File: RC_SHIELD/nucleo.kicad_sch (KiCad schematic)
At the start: 1 part

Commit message: footprints assigned
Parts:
- A1: footprint NUCLEO-F746ZG:MODULE_NUCLEO-F746ZG -> NUCLEO-F746ZG:MODULE_NUCLEO-F746ZG_no_arduino
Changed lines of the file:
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@@
       (effects (font (size 1.27 1.27)))
     )
-    (property "Footprint" "NUCLEO-F746ZG:MODULE_NUCLEO-F746ZG" (at 69.215 -38.1 0)
+    (property "Footprint" "NUCLEO-F746ZG:MODULE_NUCLEO-F746ZG_no_arduino" (at 69.215 -38.1 0)
       (effects (font (size 1.27 1.27)) (justify bottom) hide)
     )
@@
       (effects (font (size 1.27 1.27)))
     )
-    (property "Footprint" "NUCLEO-F746ZG:MODULE_NUCLEO-F746ZG" (at 259.715 -60.96 0)
+    (property "Footprint" "NUCLEO-F746ZG:MODULE_NUCLEO-F746ZG_no_arduino" (at 259.715 -60.96 0)
       (effects (font (size 1.27 1.27)) (justify bottom) hide)
     )
@@
       (effects (font (size 1.27 1.27)))
     )
-    (property "Footprint" "NUCLEO-F746ZG:MODULE_NUCLEO-F746ZG" (at 158.115 -37.465 0)
+    (property "Footprint" "NUCLEO-F746ZG:MODULE_NUCLEO-F746ZG_no_arduino" (at 158.115 -37.465 0)
       (effects (font (size 1.27 1.27)) (justify bottom) hide)
     )
@@
       (effects (font (size 1.27 1.27)))
     )
-    (property "Footprint" "NUCLEO-F746ZG:MODULE_NUCLEO-F746ZG" (at 70.485 55.245 0)
+    (property "Footprint" "NUCLEO-F746ZG:MODULE_NUCLEO-F746ZG_no_arduino" (at 70.485 55.245 0)
       (effects (font (size 1.27 1.27)) (justify bottom) hide)
     )
@@
       (effects (font (size 1.27 1.27)))
     )
-    (property "Footprint" "NUCLEO-F746ZG:MODULE_NUCLEO-F746ZG" (at 150.495 52.705 0)
+    (property "Footprint" "NUCLEO-F746ZG:MODULE_NUCLEO-F746ZG_no_arduino" (at 150.495 52.705 0)
       (effects (font (size 1.27 1.27)) (justify bottom) hide)
     )
@@
       (effects (font (size 1.27 1.27)))
     )
-    (property "Footprint" "NUCLEO-F746ZG:MODULE_NUCLEO-F746ZG" (at 260.35 20.32 0)
-      (effects (font (size 1.27 1.27)) (justify bottom) hide)
-    )
+    (property "Footprint" "NUCLEO-F746ZG:MODULE_NUCLEO-F746ZG_no_arduino" (at 260.35 20.32 0)
+      (effects (font (size 1.27 1.27)) (justify bottom) hide)
+    )

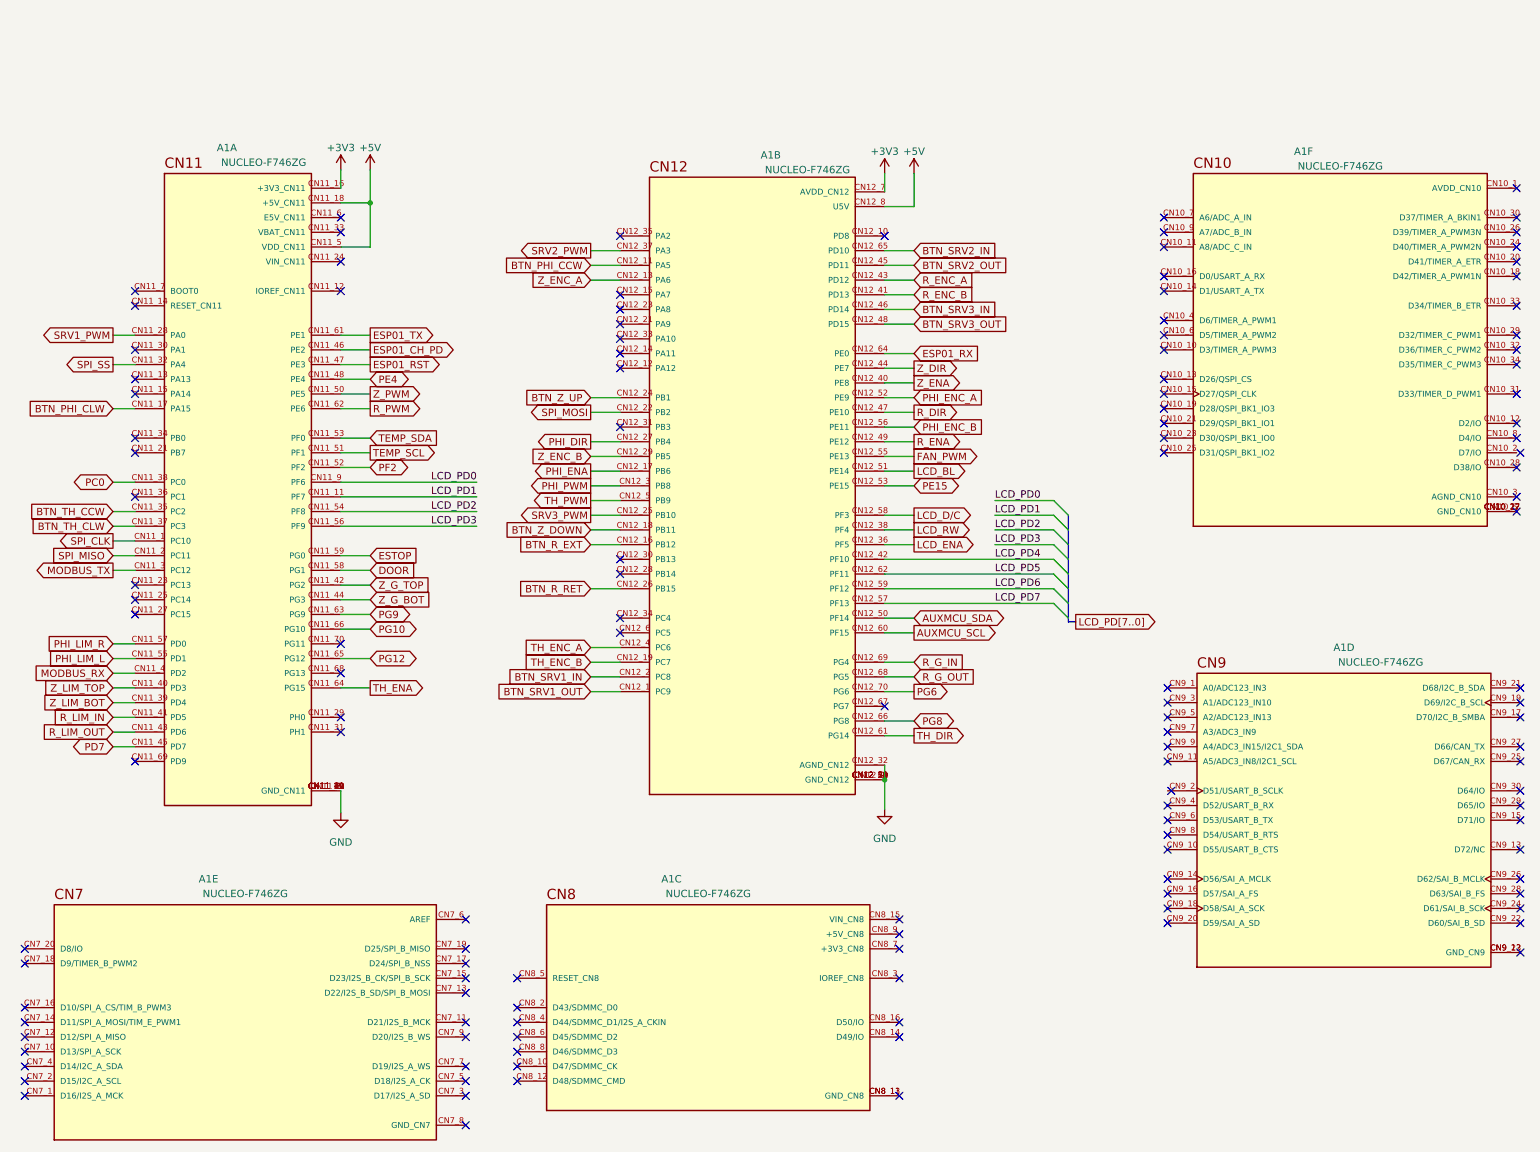
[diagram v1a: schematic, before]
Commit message: Fixed typos and names in schematic, changed optocoupler resistors; added .gitgnore file
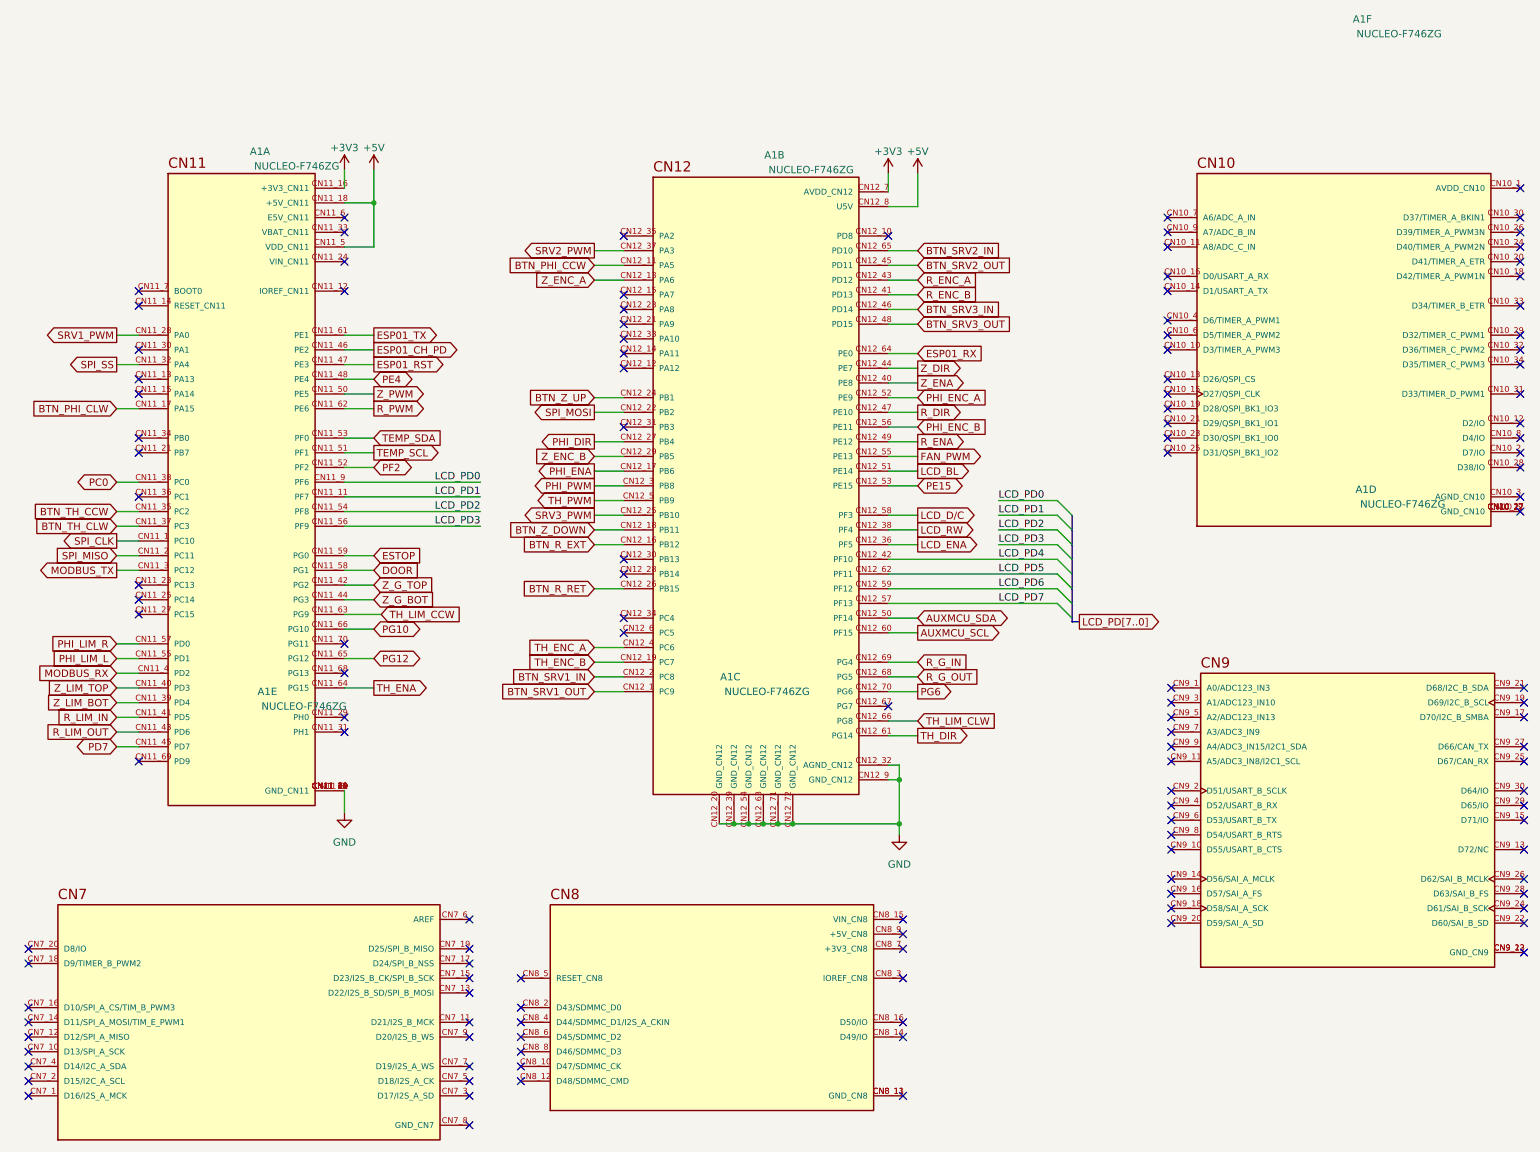
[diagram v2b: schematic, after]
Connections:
- net PG8 renamed TH_LIM_CLW
- net PG9 renamed TH_LIM_CCW
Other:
- moved on the sheet: A1A, A1C, A1D, A1E, A1F

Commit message: [SCH] reorganized optocouplers and tidied up page 2
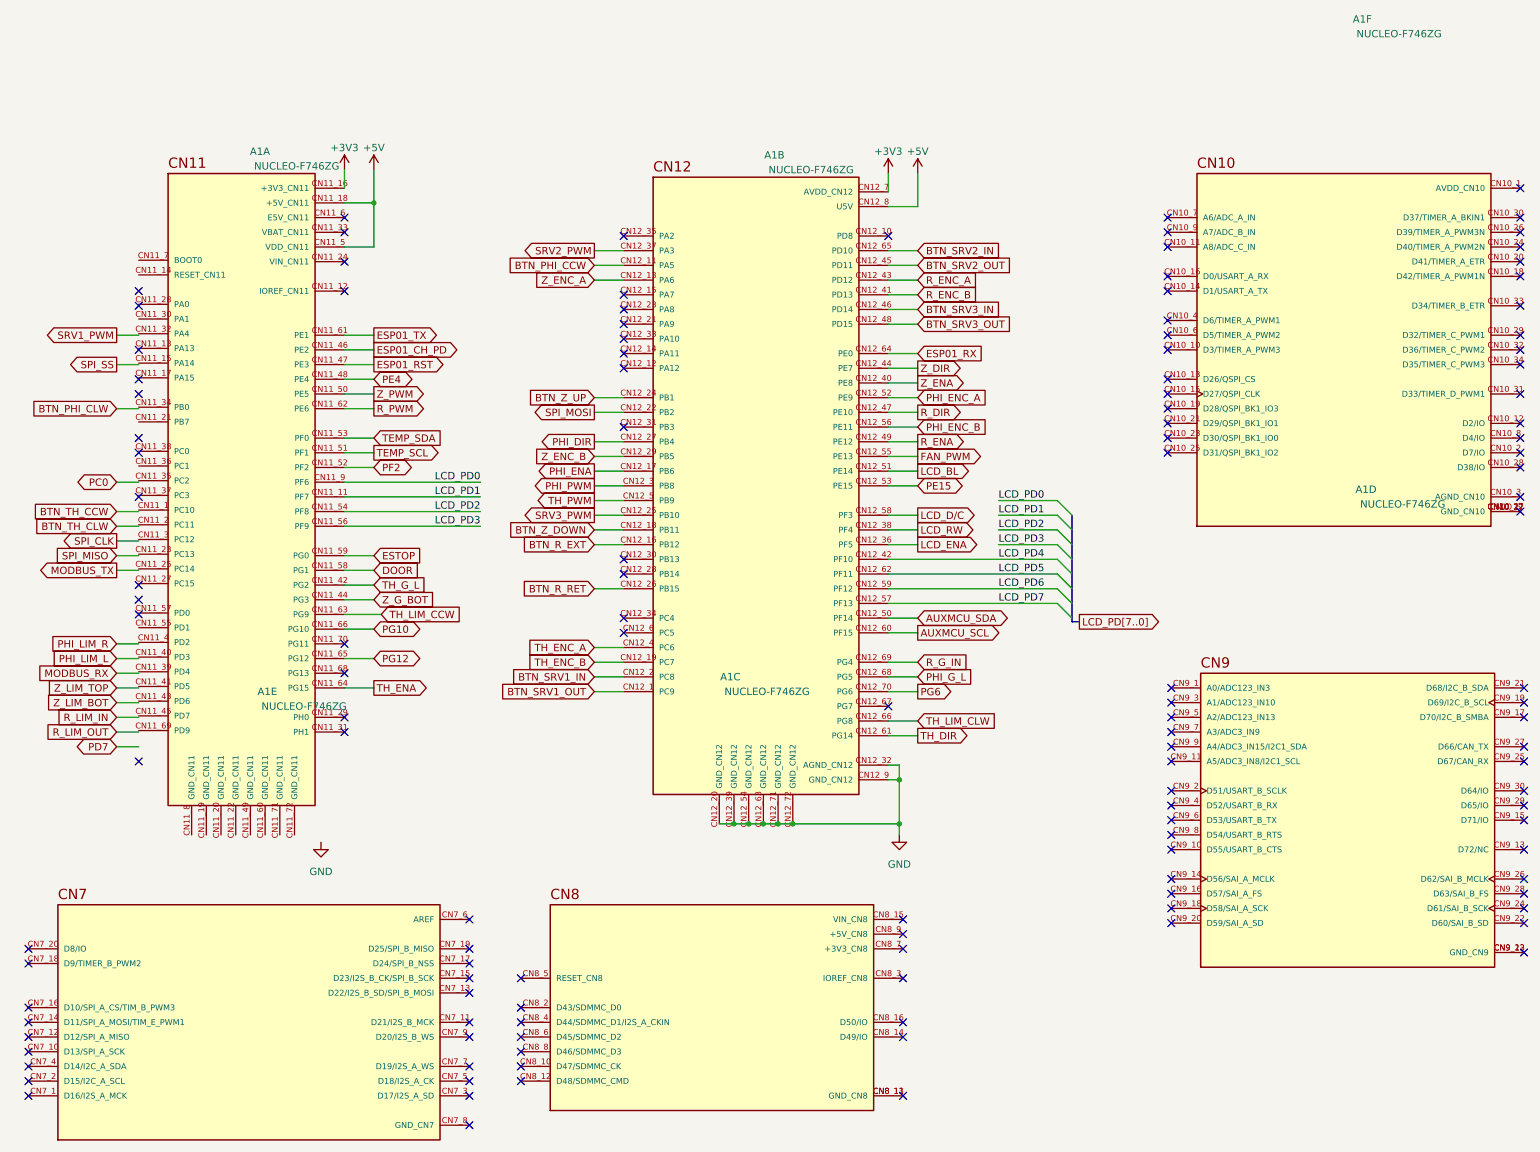
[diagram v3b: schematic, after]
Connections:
- net BTN_PHI_CLW: no longer A1.CN11_17 (PA15)
- net BTN_TH_CCW: no longer A1.CN11_35 (PC2)
- net BTN_TH_CLW: no longer A1.CN11_37 (PC3)
- net GND: no longer A1.CN11_19 (GND_CN11), A1.CN11_20 (GND_CN11), A1.CN11_22 (GND_CN11), A1.CN11_49 (GND_CN11), A1.CN11_60 (GND_CN11), A1.CN11_71 (GND_CN11), A1.CN11_72 (GND_CN11), A1.CN11_8 (GND_CN11)
- net MODBUS_RX: no longer A1.CN11_4 (PD2)
- net MODBUS_TX: no longer A1.CN11_3 (PC12)
- net PC0: no longer A1.CN11_38 (PC0)
- net PD7: no longer A1.CN11_45 (PD7)
- net PHI_LIM_L: no longer A1.CN11_55 (PD1)
- net PHI_LIM_R: no longer A1.CN11_57 (PD0)
- net R_LIM_IN: no longer A1.CN11_41 (PD5)
- net R_LIM_OUT: no longer A1.CN11_43 (PD6)
- net SPI_CLK: no longer A1.CN11_1 (PC10)
- net SPI_MISO: no longer A1.CN11_2 (PC11)
- net SPI_SS: no longer A1.CN11_32 (PA4)
- net SRV1_PWM: no longer A1.CN11_28 (PA0)
- net Z_LIM_BOT: no longer A1.CN11_39 (PD4)
- net Z_LIM_TOP: no longer A1.CN11_40 (PD3)
- net R_G_OUT renamed PHI_G_L
- net Z_G_TOP renamed TH_G_L
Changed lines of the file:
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@@
-    (stroke (width 0) (type default))
-  )
-  (wire (pts (xy 73.66 129.54) (xy 73.66 133.35))
     (stroke (width 0) (type default))
   )
@@
     )
   )
-  (global_label "R_G_OUT" (shape input) (at 172.72 109.855 0)
+  (global_label "PHI_G_L" (shape input) (at 172.72 109.855 0)
     (effects (font (size 1.27 1.27)) (justify left))
     (property "Intersheetrefs" "${INTERSHEET_REFS}" (at 182.88 109.855 0)
@@
     )
   )
-  (global_label "Z_G_TOP" (shape input) (at 78.74 93.98 0)
+  (global_label "TH_G_L" (shape input) (at 78.74 93.98 0)
     (effects (font (size 1.27 1.27)) (justify left))
     (property "Intersheetrefs" "${INTERSHEET_REFS}" (at 88.779 93.98 0)
@@
     )
   )
-  (symbol (lib_id "power:GND") (at 73.66 133.35 0) (unit 1)
+  (symbol (lib_id "power:GND") (at 69.596 138.43 0) (unit 1)
     (in_bom yes) (on_board yes) (dnp no) (fields_autoplaced)
-    (property "Reference" "#PWR02" (at 73.66 139.7 0)
+    (property "Reference" "#PWR02" (at 69.596 144.78 0)
       (effects (font (size 1.27 1.27)) hide)
     )
-    (property "Value" "GND" (at 73.66 138.43 0)
+    (property "Value" "GND" (at 69.596 143.51 0)
       (effects (font (size 1.27 1.27)))
     )
-    (property "Footprint" "" (at 73.66 133.35 0)
+    (property "Footprint" "" (at 69.596 138.43 0)
       (effects (font (size 1.27 1.27)) hide)
     )
-    (property "Datasheet" "" (at 73.66 133.35 0)
+    (property "Datasheet" "" (at 69.596 138.43 0)
       (effects (font (size 1.27 1.27)) hide)
     )

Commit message: [SCH] added "exclude from BOM" signs
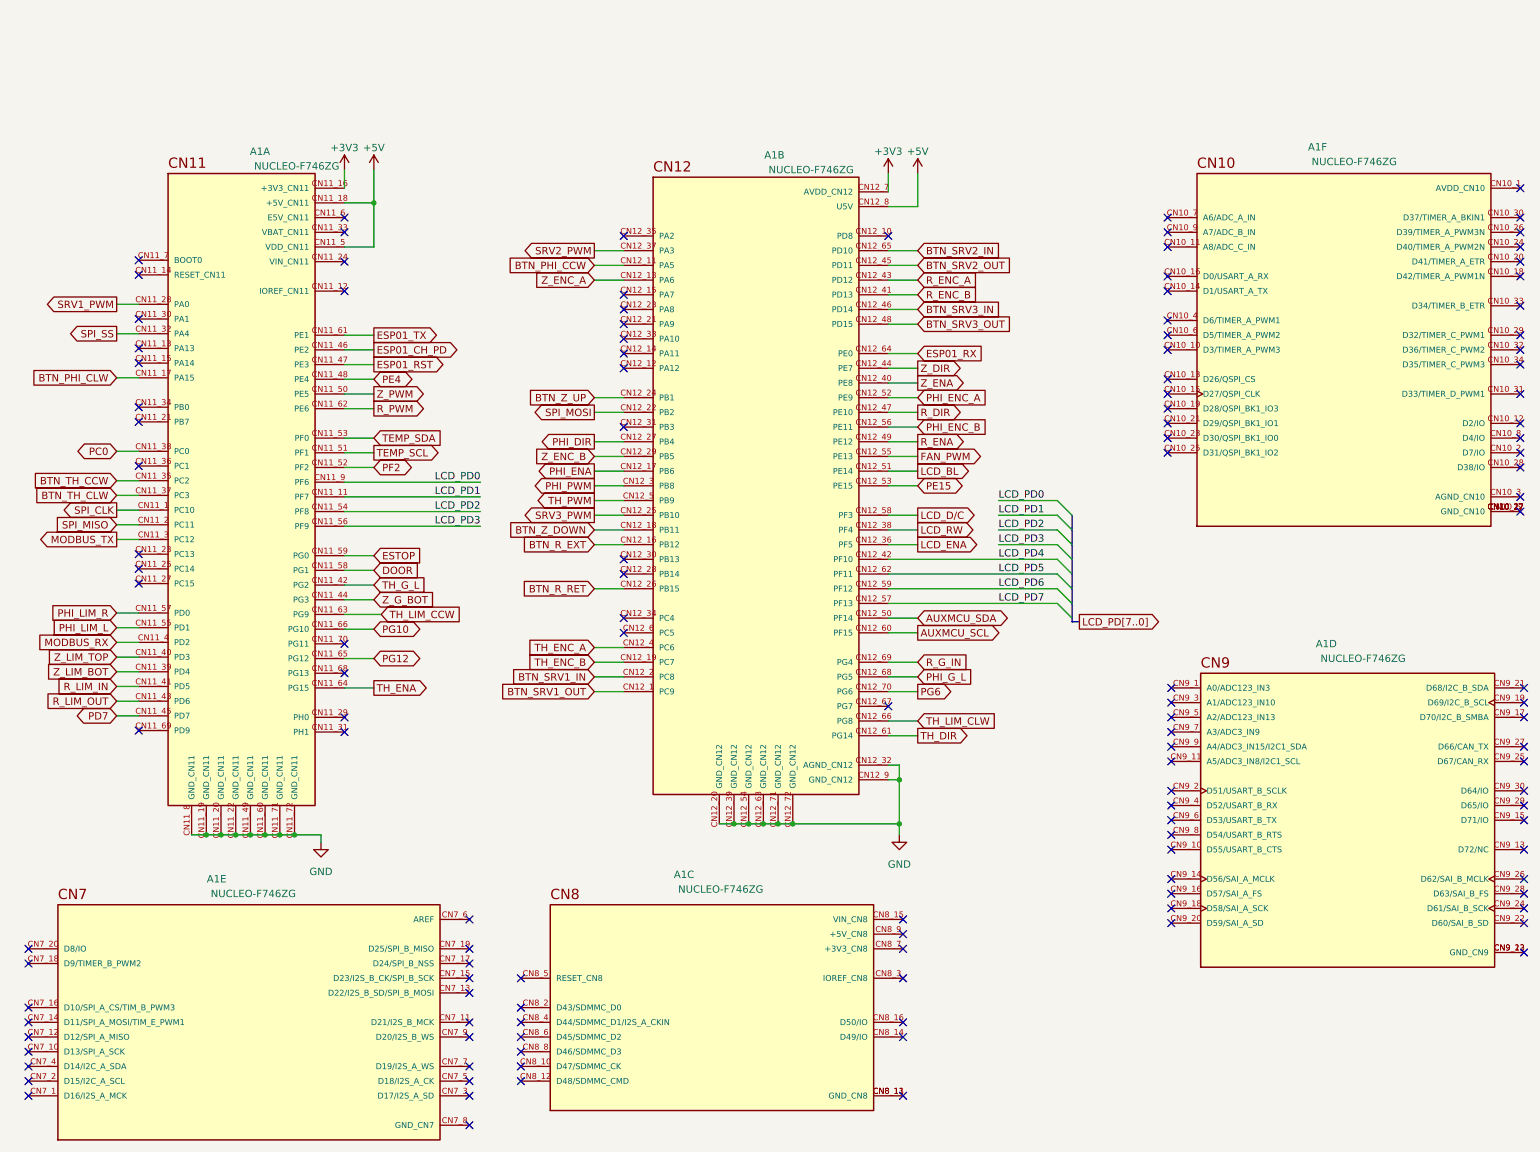
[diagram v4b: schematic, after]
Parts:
- A1: now left out of the parts list
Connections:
- net BTN_PHI_CLW: now also A1.CN11_17 (PA15)
- net BTN_TH_CCW: now also A1.CN11_35 (PC2)
- net BTN_TH_CLW: now also A1.CN11_37 (PC3)
- net GND: now also A1.CN11_19 (GND_CN11), A1.CN11_20 (GND_CN11), A1.CN11_22 (GND_CN11), A1.CN11_49 (GND_CN11), A1.CN11_60 (GND_CN11), A1.CN11_71 (GND_CN11), A1.CN11_72 (GND_CN11), A1.CN11_8 (GND_CN11)
- net MODBUS_RX: now also A1.CN11_4 (PD2)
- net MODBUS_TX: now also A1.CN11_3 (PC12)
- net PC0: now also A1.CN11_38 (PC0)
- net PD7: now also A1.CN11_45 (PD7)
- net PHI_LIM_L: now also A1.CN11_55 (PD1)
- net PHI_LIM_R: now also A1.CN11_57 (PD0)
- net R_LIM_IN: now also A1.CN11_41 (PD5)
- net R_LIM_OUT: now also A1.CN11_43 (PD6)
- net SPI_CLK: now also A1.CN11_1 (PC10)
- net SPI_MISO: now also A1.CN11_2 (PC11)
- net SPI_SS: now also A1.CN11_32 (PA4)
- net SRV1_PWM: now also A1.CN11_28 (PA0)
- net Z_LIM_BOT: now also A1.CN11_39 (PD4)
- net Z_LIM_TOP: now also A1.CN11_40 (PD3)
